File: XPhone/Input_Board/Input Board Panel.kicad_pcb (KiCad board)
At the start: 2 copper layers, 100 x 100 mm, 380 parts, among them J1 AUDIO, J10 ENV, J11 PULSE, J12 PULSE, J13 Power In, J14 Power Out, J2 AUDIO, J3 ENV, J4 ENV, J5 PULSE, J6 PULSE, J7 AUDIO, J8 AUDIO, J9 ENV, Q1 BC847CW, Q2 BC847CW, Q3 BC847CW, Q4 BC847CW, Q5 BC847CW, Q6 BC847CW, Q7 BC847CW, Q8 BC847CW, Q9 BC847CW, U1 LM833, U2 78L05, U3 TL084, U4 74HC14, U5 LM833

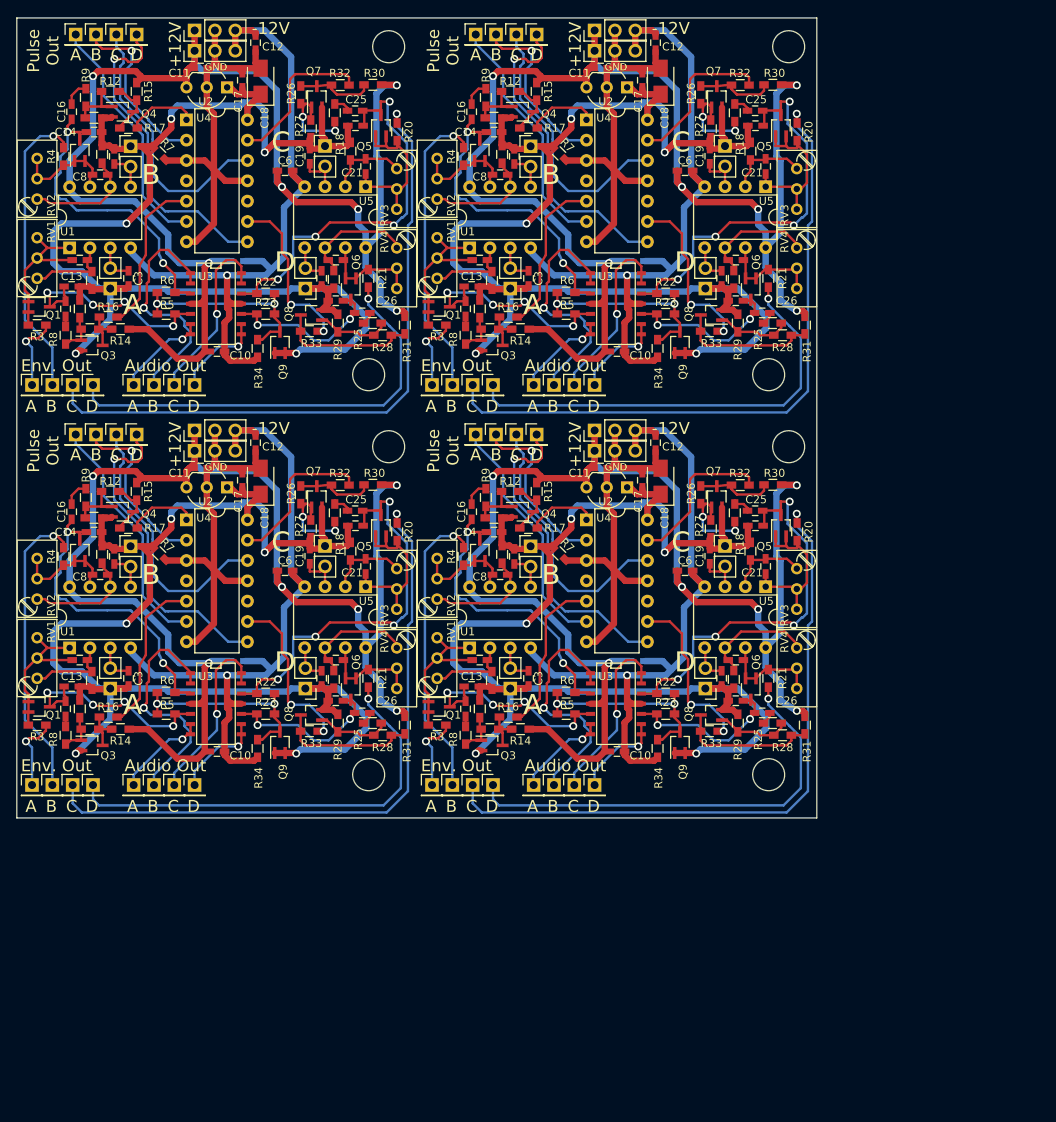
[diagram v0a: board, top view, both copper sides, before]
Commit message: fixed generation of panel
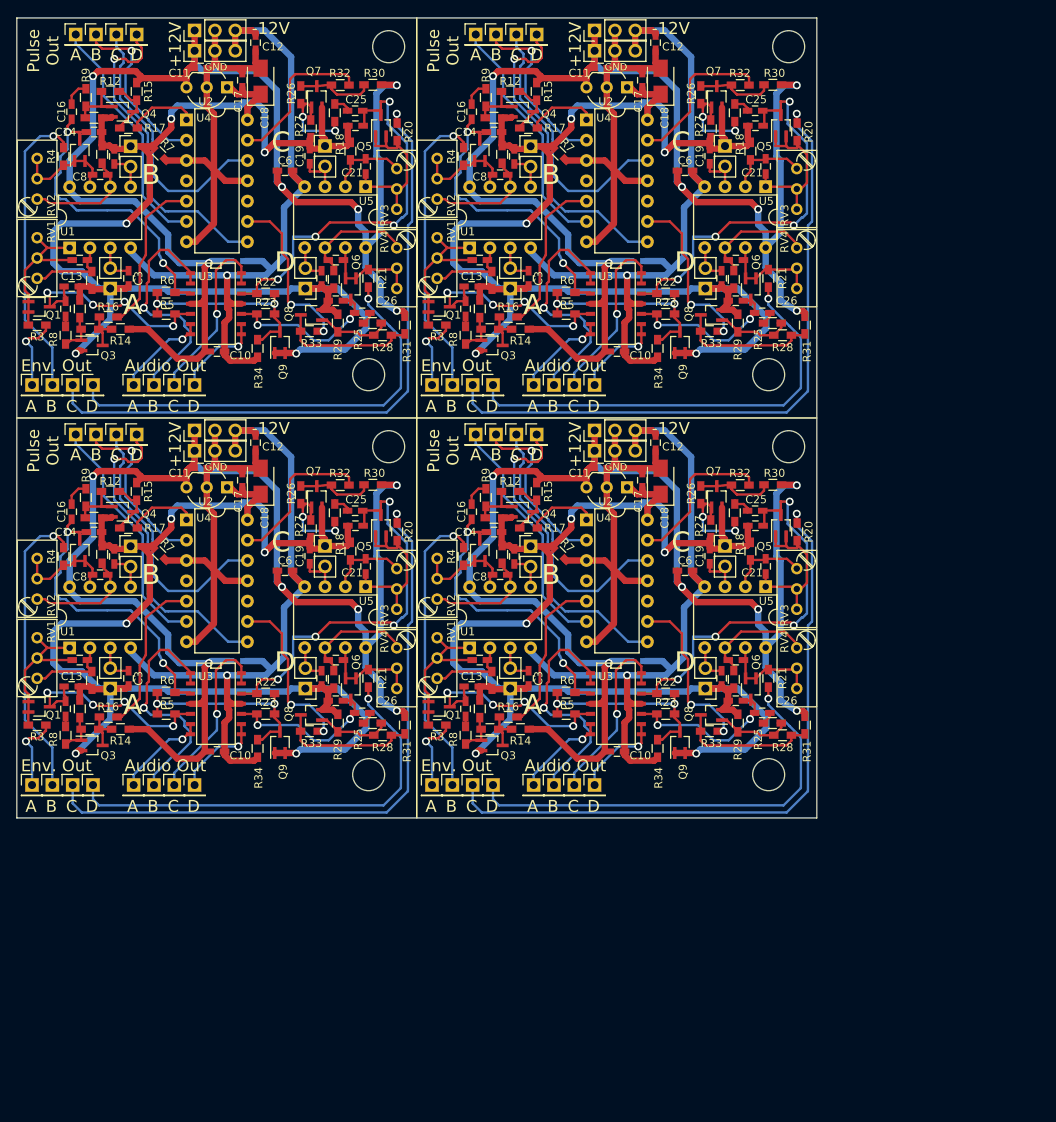
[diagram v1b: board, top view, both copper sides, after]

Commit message: optimizing XPhone/Input Board layout for cutting it into pieces; traces routed not so close to the board
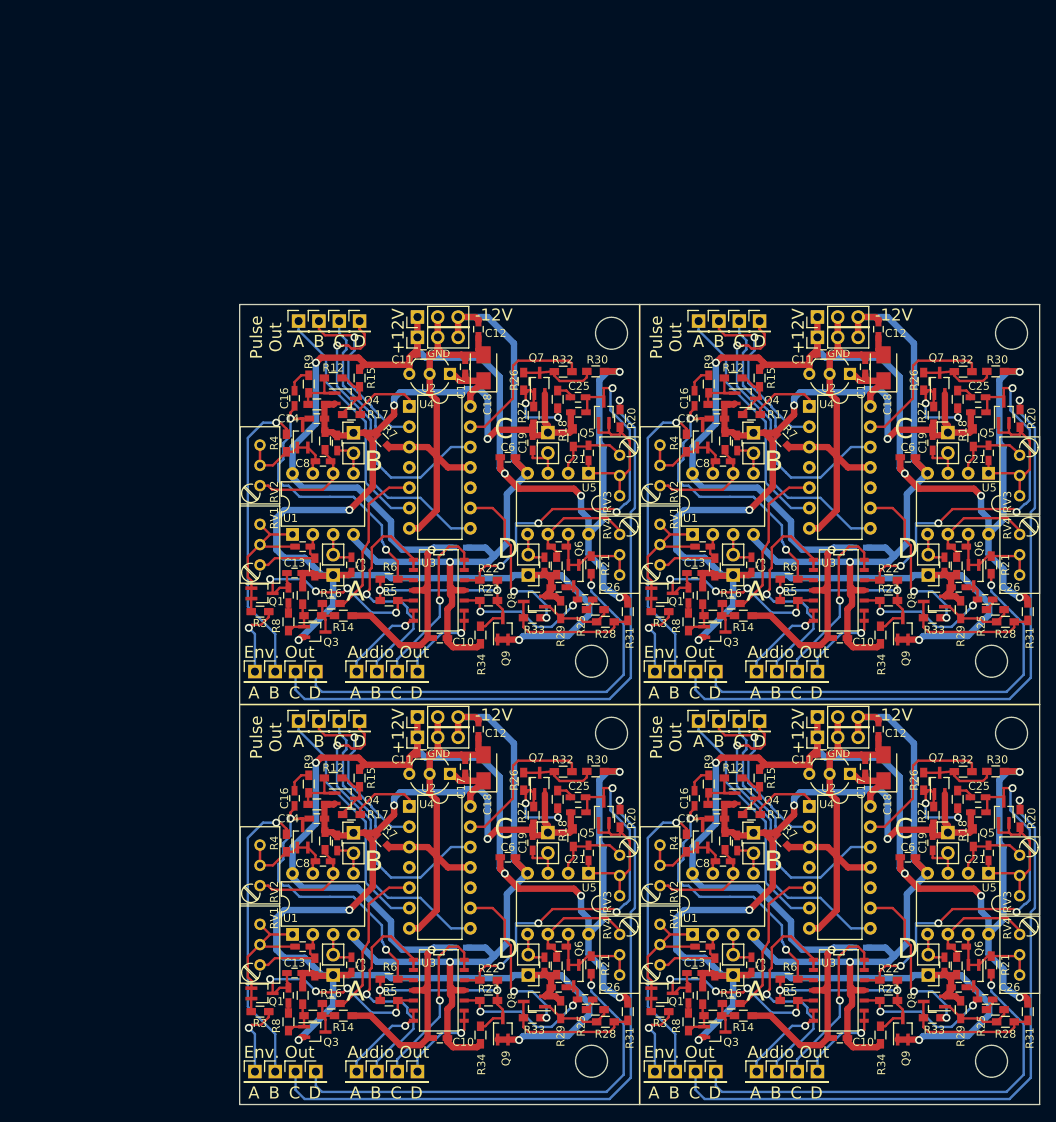
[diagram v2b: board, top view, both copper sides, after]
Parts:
- removed the C1 at (77.6, 80.4)
- removed the C1 at (27.6, 80.4)
- removed the C1 at (77.6, 30.4)
- removed the C10 at (75.0, 91.7)
- removed the C10 at (25.0, 91.7)
- removed the C10 at (75.0, 41.7)
- removed the C11 at (73.0, 56.3)
- removed the C11 at (23.0, 56.3)
- removed the C11 at (73.0, 6.26)
- removed the C12 at (79.8, 53.1)
- removed the C12 at (29.8, 53.1)
- removed the C12 at (79.8, 3.09)
- removed the C13 at (56.9, 83.6)
- removed the C13 at (6.86, 83.6)
- removed the C13 at (56.9, 33.6)
- removed the C14 at (59.7, 64.3)
- removed the C14 at (9.65, 64.3)
- removed the C14 at (59.7, 14.3)
- removed the C15 at (56.1, 86.4)
- removed the C15 at (6.10, 86.4)
- removed the C15 at (56.1, 36.4)
- removed the C16 at (56.9, 61.7)
- removed the C16 at (6.86, 61.7)
- removed the C16 at (56.9, 11.7)
- removed the C17 at (78.2, 57.8)
- removed the C17 at (28.2, 57.8)
- removed the C17 at (78.2, 7.79)
- removed the C18 at (80.5, 57.9)
- removed the C18 at (30.5, 57.9)
- removed the C18 at (80.5, 7.91)
- removed the C19 at (86.6, 67.3)
- removed the C19 at (36.6, 67.3)
- removed the C19 at (86.6, 17.3)
- removed the C20 at (88.1, 82.5)
- removed the C20 at (38.1, 82.5)
- removed the C20 at (88.1, 32.5)
- removed the C21 at (93.6, 68.6)
- removed the C21 at (43.6, 68.6)
- removed the C21 at (93.6, 18.6)
- removed the C22 at (89.9, 80.3)
- removed the C22 at (39.9, 80.3)
- removed the C22 at (89.9, 30.3)
- removed the C23 at (92.3, 63.5)
- removed the C23 at (42.3, 63.5)
- removed the C23 at (92.3, 13.5)
- removed the C24 at (89.9, 85.3)
- removed the C24 at (39.9, 85.3)
- removed the C24 at (89.9, 35.3)
- removed the C25 at (92.3, 61.6)
- removed the C25 at (42.3, 61.6)
- removed the C25 at (92.3, 11.6)
- removed the C26 at (93.2, 86.9)
- removed the C26 at (43.2, 86.9)
- removed the C26 at (93.2, 36.9)
- removed the C3 at (64.0, 82.5)
- removed the C3 at (14.0, 82.5)
- removed the C3 at (64.0, 32.5)
- removed the C4 at (62.2, 67.3)
- removed the C4 at (12.2, 67.3)
- removed the C4 at (62.2, 17.3)
- removed the C6 at (83.5, 69.1)
- removed the C6 at (33.5, 69.1)
- removed the C6 at (83.5, 19.1)
- removed the C7 at (57.9, 80.3)
- removed the C7 at (7.87, 80.3)
- removed the C7 at (57.9, 30.3)
- removed the C8 at (60.4, 69.6)
- removed the C8 at (10.4, 69.6)
- removed the C8 at (60.4, 19.6)
- removed the J1 at (51.9, 95.9)
- removed the J1 at (1.91, 95.9)
- removed the J1 at (51.9, 45.9)
- removed the J10 at (72.2, 95.9)
- removed the J10 at (22.2, 95.9)
- removed the J10 at (72.2, 45.9)
- removed the J11 at (62.4, 52.1)
- removed the J11 at (12.4, 52.1)
- removed the J11 at (62.4, 2.07)
- removed the J12 at (65.0, 52.1)
- removed the J12 at (15.0, 52.1)
- removed the J12 at (65.0, 2.07)
- removed the J13 at (72.2, 51.6)
- removed the J13 at (22.2, 51.6)
- removed the J13 at (72.2, 1.56)
- removed the J14 at (72.2, 54.1)
- removed the J14 at (22.2, 54.1)
- removed the J14 at (72.2, 4.10)
- removed the J2 at (54.4, 95.9)
- removed the J2 at (4.45, 95.9)
- removed the J2 at (54.4, 45.9)
- removed the J3 at (64.6, 95.9)
- removed the J3 at (14.6, 95.9)
- removed the J3 at (64.6, 45.9)
- removed the J4 at (67.1, 95.9)
- removed the J4 at (17.1, 95.9)
- removed the J4 at (67.1, 45.9)
- removed the J5 at (57.4, 52.1)
- removed the J5 at (7.37, 52.1)
- removed the J5 at (57.4, 2.07)
- removed the J6 at (59.9, 52.1)
- removed the J6 at (9.91, 52.1)
- removed the J6 at (59.9, 2.07)
- removed the J7 at (57.0, 95.9)
- removed the J7 at (6.99, 95.9)
- removed the J7 at (57.0, 45.9)
- removed the J8 at (59.5, 95.9)
- removed the J8 at (9.53, 95.9)
- removed the J8 at (59.5, 45.9)
- removed the J9 at (69.7, 95.9)
- removed the J9 at (19.7, 95.9)
- removed the J9 at (69.7, 45.9)
- removed the L1 at (61.7, 83.8)
- removed the L1 at (11.7, 83.8)
- removed the L1 at (61.7, 33.8)
- removed the L2 at (64.2, 66.0)
- removed the L2 at (14.2, 66.0)
- removed the L2 at (64.2, 16.0)
- removed the L3 at (88.5, 66.0)
- removed the L3 at (38.5, 66.0)
- removed the L3 at (88.5, 16.0)
- removed the L4 at (86.1, 83.8)
- removed the L4 at (36.1, 83.8)
- removed the L4 at (86.1, 33.8)
- removed the Q1 at (52.8, 86.1)
- removed the Q1 at (2.79, 86.1)
- removed the Q1 at (52.8, 36.1)
- removed the Q2 at (57.9, 66.5)
- removed the Q2 at (7.87, 66.5)
- removed the Q2 at (57.9, 16.5)
- removed the Q3 at (59.4, 90.9)
- removed the Q3 at (9.40, 90.9)
- removed the Q3 at (59.4, 40.9)
- removed the Q4 at (63.2, 61.7)
- removed the Q4 at (13.2, 61.7)
- removed the Q4 at (63.2, 11.7)
- removed the Q5 at (95.5, 63.5)
- removed the Q5 at (45.5, 63.5)
- removed the Q5 at (95.5, 13.5)
- removed the Q6 at (91.7, 83.9)
- removed the Q6 at (41.7, 83.9)
- removed the Q6 at (91.7, 33.9)
- removed the Q7 at (87.5, 59.9)
- removed the Q7 at (37.5, 59.9)
- removed the Q7 at (87.5, 9.86)
- removed the Q8 at (86.8, 87.1)
- removed the Q8 at (36.8, 87.1)
- removed the Q8 at (86.8, 37.1)
- removed the Q9 at (82.9, 90.6)
- removed the Q9 at (32.9, 90.6)
- removed the Q9 at (82.9, 40.6)
- removed the R1 at (59.4, 82.8)
- removed the R1 at (9.40, 82.8)
- removed the R1 at (59.4, 32.8)
- removed the R10 at (59.1, 88.9)
- removed the R10 at (9.14, 88.9)
- removed the R10 at (59.1, 38.9)
- removed the R11 at (57.9, 86.4)
- removed the R11 at (7.87, 86.4)
- removed the R11 at (57.9, 36.4)
- removed the R12 at (61.7, 59.2)
- removed the R12 at (11.7, 59.2)
- removed the R12 at (61.7, 9.18)
- removed the R13 at (59.7, 62.5)
- removed the R13 at (9.65, 62.5)
- removed the R13 at (59.7, 12.5)
- removed the R14 at (63.0, 88.9)
- removed the R14 at (13.0, 88.9)
- removed the R14 at (63.0, 38.9)
- removed the R15 at (65.0, 59.2)
- removed the R15 at (15.0, 59.2)
- removed the R15 at (65.0, 9.18)
- removed the R16 at (61.4, 87.4)
- removed the R16 at (11.4, 87.4)
- removed the R16 at (61.4, 37.4)
- removed the R17 at (64.0, 63.8)
- removed the R17 at (14.0, 63.8)
- removed the R17 at (64.0, 13.8)
- removed the R18 at (91.7, 66.6)
- removed the R18 at (41.7, 66.6)
- removed the R18 at (91.7, 16.6)
- removed the R19 at (89.6, 82.7)
- removed the R19 at (39.6, 82.7)
- removed the R19 at (89.6, 32.7)
- removed the R2 at (60.7, 67.1)
- removed the R2 at (10.7, 67.1)
- removed the R2 at (60.7, 17.1)
- removed the R20 at (97.5, 64.2)
- removed the R20 at (47.5, 64.2)
- removed the R20 at (97.5, 14.2)
- removed the R21 at (93.9, 82.5)
- removed the R21 at (43.9, 82.5)
- removed the R21 at (93.9, 32.5)
- removed the R22 at (81.1, 84.5)
- removed the R22 at (31.1, 84.5)
- removed the R22 at (81.1, 34.5)
- removed the R23 at (81.1, 87.0)
- removed the R23 at (31.1, 87.0)
- removed the R23 at (81.1, 37.0)
- removed the R24 at (89.8, 61.9)
- removed the R24 at (39.8, 61.9)
- removed the R24 at (89.8, 11.9)
- removed the R25 at (94.5, 88.1)
- removed the R25 at (44.5, 88.1)
- removed the R25 at (94.5, 38.1)
- removed the R26 at (85.5, 59.6)
- removed the R26 at (35.5, 59.6)
- removed the R26 at (85.5, 9.61)
- removed the R27 at (86.8, 63.9)
- removed the R27 at (36.8, 63.9)
- removed the R27 at (86.8, 13.9)
- removed the R28 at (95.7, 89.7)
- removed the R28 at (45.7, 89.7)
- removed the R28 at (95.7, 39.7)
- removed the R29 at (90.1, 88.1)
- removed the R29 at (40.1, 88.1)
- removed the R29 at (90.1, 38.1)
- removed the R3 at (52.5, 88.4)
- removed the R3 at (2.54, 88.4)
- removed the R3 at (52.5, 38.4)
- removed the R30 at (94.5, 58.4)
- removed the R30 at (44.5, 58.4)
- removed the R30 at (94.5, 8.36)
- removed the R31 at (98.5, 88.4)
- removed the R31 at (48.5, 88.4)
- removed the R31 at (98.5, 38.4)
- removed the R32 at (90.4, 58.4)
- removed the R32 at (40.4, 58.4)
- removed the R32 at (90.4, 8.39)
- removed the R33 at (86.6, 89.2)
- removed the R33 at (36.6, 89.2)
- removed the R33 at (86.6, 39.2)
- removed the R34 at (80.1, 91.3)
- removed the R34 at (30.1, 91.3)
- removed the R34 at (80.1, 41.3)
- removed the R4 at (55.8, 67.3)
- removed the R4 at (5.84, 67.3)
- removed the R4 at (55.8, 17.3)
- removed the R5 at (68.7, 87.0)
- removed the R5 at (18.7, 87.0)
- removed the R5 at (68.7, 37.0)
- removed the R6 at (68.7, 84.3)
- removed the R6 at (18.7, 84.3)
- removed the R6 at (68.7, 34.3)
- removed the R7 at (67.8, 66.9)
- removed the R7 at (17.8, 66.9)
- removed the R7 at (67.8, 16.9)
- removed the R8 at (56.1, 89.7)
- removed the R8 at (6.10, 89.7)
- removed the R8 at (56.1, 39.7)
- removed the R9 at (58.6, 59.9)
- removed the R9 at (8.64, 59.9)
- removed the R9 at (58.6, 9.94)
- removed the REF** at (94.0, 94.6)
- removed the REF** at (44.0, 94.6)
- removed the REF** at (94.0, 44.6)
- removed the REF** at (96.5, 53.6)
- removed the REF** at (46.5, 53.6)
- removed the REF** at (96.5, 3.59)
- removed the RV1 at (52.5, 82.5)
- removed the RV1 at (2.54, 82.5)
- removed the RV1 at (52.5, 32.5)
- removed the RV2 at (52.5, 72.6)
- removed the RV2 at (2.54, 72.6)
- removed the RV2 at (52.5, 22.6)
- removed the RV3 at (97.5, 68.8)
- removed the RV3 at (47.5, 68.8)
- removed the RV3 at (97.5, 18.8)
- removed the RV4 at (97.5, 78.7)
- removed the RV4 at (47.5, 78.7)
- removed the RV4 at (97.5, 28.7)
- removed the U1 at (56.6, 78.7)
- removed the U1 at (6.60, 78.7)
- removed the U1 at (56.6, 28.7)
- removed the U2 at (76.3, 58.7)
- removed the U2 at (26.3, 58.7)
- removed the U2 at (76.3, 8.67)
- removed the U3 at (75.0, 85.7)
- removed the U3 at (25.0, 85.7)
- removed the U3 at (75.0, 35.7)
- removed the U4 at (71.2, 62.7)
- removed the U4 at (21.2, 62.7)
- removed the U4 at (71.2, 12.7)
- removed the U5 at (93.6, 71.1)
- removed the U5 at (43.6, 71.1)
- removed the U5 at (93.6, 21.1)
- added C1: 10n, Capacitors_SMD:C_0603_HandSoldering, B.Cu at (105.4, 116.2)
- added C1: 10n, Capacitors_SMD:C_0603_HandSoldering, B.Cu at (55.4, 116.2)
- added C1: 10n, Capacitors_SMD:C_0603_HandSoldering, B.Cu at (105.4, 66.2)
- added C10: 10n, Capacitors_SMD:C_0603_HandSoldering, F.Cu at (102.9, 127.5)
- added C10: 10n, Capacitors_SMD:C_0603_HandSoldering, F.Cu at (52.9, 127.5)
- added C10: 10n, Capacitors_SMD:C_0603_HandSoldering, F.Cu at (102.9, 77.5)
- added C11: 10n, Capacitors_SMD:C_0603_HandSoldering, F.Cu at (100.8, 92.1)
- added C11: 10n, Capacitors_SMD:C_0603_HandSoldering, F.Cu at (50.8, 92.1)
- added C11: 10n, Capacitors_SMD:C_0603_HandSoldering, F.Cu at (100.8, 42.1)
- added C12: 10n, Capacitors_SMD:C_0603_HandSoldering, F.Cu at (107.7, 88.9)
- added C12: 10n, Capacitors_SMD:C_0603_HandSoldering, F.Cu at (57.7, 88.9)
- added C12: 10n, Capacitors_SMD:C_0603_HandSoldering, F.Cu at (107.7, 38.9)
- added C13: 10n, Capacitors_SMD:C_0603_HandSoldering, F.Cu at (84.7, 119.4)
- added C13: 10n, Capacitors_SMD:C_0603_HandSoldering, F.Cu at (34.7, 119.4)
- added C13: 10n, Capacitors_SMD:C_0603_HandSoldering, F.Cu at (84.7, 69.4)
- added C14: 10n, Capacitors_SMD:C_0603_HandSoldering, F.Cu at (87.5, 100.1)
- added C14: 10n, Capacitors_SMD:C_0603_HandSoldering, F.Cu at (37.5, 100.1)
- added C14: 10n, Capacitors_SMD:C_0603_HandSoldering, F.Cu at (87.5, 50.1)
- added C15: 10n, Capacitors_SMD:C_0603_HandSoldering, F.Cu at (84.0, 122.2)
- added C15: 10n, Capacitors_SMD:C_0603_HandSoldering, F.Cu at (34.0, 122.2)
- added C15: 10n, Capacitors_SMD:C_0603_HandSoldering, F.Cu at (84.0, 72.2)
- added C16: 10n, Capacitors_SMD:C_0603_HandSoldering, F.Cu at (84.7, 97.5)
- added C16: 10n, Capacitors_SMD:C_0603_HandSoldering, F.Cu at (34.7, 97.5)
- added C16: 10n, Capacitors_SMD:C_0603_HandSoldering, F.Cu at (84.7, 47.5)
- added C17: 10n, Capacitors_SMD:C_0603_HandSoldering, F.Cu at (106.1, 93.6)
- added C17: 10n, Capacitors_SMD:C_0603_HandSoldering, F.Cu at (56.1, 93.6)
- added C17: 10n, Capacitors_SMD:C_0603_HandSoldering, F.Cu at (106.1, 43.6)
- added C18: 10µ, Capacitors_Tantalum_SMD:CP_Tantalum_Case-B_EIA-3528-21_Wave, F.Cu at (108.3, 93.7)
- added C18: 10µ, Capacitors_Tantalum_SMD:CP_Tantalum_Case-B_EIA-3528-21_Wave, F.Cu at (58.3, 93.7)
- added C18: 10µ, Capacitors_Tantalum_SMD:CP_Tantalum_Case-B_EIA-3528-21_Wave, F.Cu at (108.3, 43.7)
- added C19: 10n, Capacitors_SMD:C_0603_HandSoldering, F.Cu at (114.5, 103.1)
- added C19: 10n, Capacitors_SMD:C_0603_HandSoldering, F.Cu at (64.5, 103.1)
- added C19: 10n, Capacitors_SMD:C_0603_HandSoldering, F.Cu at (114.5, 53.1)
- added C20: 10n, Capacitors_SMD:C_0603_HandSoldering, F.Cu at (116.0, 118.4)
- added C20: 10n, Capacitors_SMD:C_0603_HandSoldering, F.Cu at (66.0, 118.4)
- added C20: 10n, Capacitors_SMD:C_0603_HandSoldering, F.Cu at (116.0, 68.4)
- added C21: 10n, Capacitors_SMD:C_0603_HandSoldering, F.Cu at (121.5, 104.4)
- added C21: 10n, Capacitors_SMD:C_0603_HandSoldering, F.Cu at (71.5, 104.4)
- added C21: 10n, Capacitors_SMD:C_0603_HandSoldering, F.Cu at (121.5, 54.4)
- added C22: 10n, Capacitors_SMD:C_0603_HandSoldering, F.Cu at (117.7, 116.1)
- added C22: 10n, Capacitors_SMD:C_0603_HandSoldering, F.Cu at (67.7, 116.1)
- added C22: 10n, Capacitors_SMD:C_0603_HandSoldering, F.Cu at (117.7, 66.1)
- added C23: 10n, Capacitors_SMD:C_0603_HandSoldering, F.Cu at (120.2, 99.3)
- added C23: 10n, Capacitors_SMD:C_0603_HandSoldering, F.Cu at (70.2, 99.3)
- added C23: 10n, Capacitors_SMD:C_0603_HandSoldering, F.Cu at (120.2, 49.3)
- added C24: 10n, Capacitors_SMD:C_0603_HandSoldering, F.Cu at (117.7, 121.2)
- added C24: 10n, Capacitors_SMD:C_0603_HandSoldering, F.Cu at (67.7, 121.2)
- added C24: 10n, Capacitors_SMD:C_0603_HandSoldering, F.Cu at (117.7, 71.2)
- added C25: 10n, Capacitors_SMD:C_0603_HandSoldering, F.Cu at (120.2, 97.4)
- added C25: 10n, Capacitors_SMD:C_0603_HandSoldering, F.Cu at (70.2, 97.4)
- added C25: 10n, Capacitors_SMD:C_0603_HandSoldering, F.Cu at (120.2, 47.4)
- added C26: 10n, Capacitors_SMD:C_0603_HandSoldering, F.Cu at (121.0, 122.7)
- added C26: 10n, Capacitors_SMD:C_0603_HandSoldering, F.Cu at (71.0, 122.7)
- added C26: 10n, Capacitors_SMD:C_0603_HandSoldering, F.Cu at (121.0, 72.7)
- added C3: 10n, Capacitors_SMD:C_0603_HandSoldering, F.Cu at (91.8, 118.4)
- added C3: 10n, Capacitors_SMD:C_0603_HandSoldering, F.Cu at (41.8, 118.4)
- added C3: 10n, Capacitors_SMD:C_0603_HandSoldering, F.Cu at (91.8, 68.4)
- added C4: 10n, Capacitors_SMD:C_0603_HandSoldering, F.Cu at (90.1, 103.1)
- added C4: 10n, Capacitors_SMD:C_0603_HandSoldering, F.Cu at (40.1, 103.1)
- added C4: 10n, Capacitors_SMD:C_0603_HandSoldering, F.Cu at (90.1, 53.1)
- added C6: 10n, Capacitors_SMD:C_0603_HandSoldering, F.Cu at (111.4, 104.9)
- added C6: 10n, Capacitors_SMD:C_0603_HandSoldering, F.Cu at (61.4, 104.9)
- added C6: 10n, Capacitors_SMD:C_0603_HandSoldering, F.Cu at (111.4, 54.9)
- added C7: 10n, Capacitors_SMD:C_0603_HandSoldering, F.Cu at (85.7, 116.1)
- added C7: 10n, Capacitors_SMD:C_0603_HandSoldering, F.Cu at (35.7, 116.1)
- added C7: 10n, Capacitors_SMD:C_0603_HandSoldering, F.Cu at (85.7, 66.1)
- added C8: 10n, Capacitors_SMD:C_0603_HandSoldering, F.Cu at (88.3, 105.4)
- added C8: 10n, Capacitors_SMD:C_0603_HandSoldering, F.Cu at (38.3, 105.4)
- added C8: 10n, Capacitors_SMD:C_0603_HandSoldering, F.Cu at (88.3, 55.4)
- added J1: AUDIO, Pin_Headers:Pin_Header_Straight_1x01_Pitch2.54mm, F.Cu at (79.8, 131.7)
- added J1: AUDIO, Pin_Headers:Pin_Header_Straight_1x01_Pitch2.54mm, F.Cu at (29.8, 131.7)
- added J1: AUDIO, Pin_Headers:Pin_Header_Straight_1x01_Pitch2.54mm, F.Cu at (79.8, 81.7)
- added J10: ENV, Pin_Headers:Pin_Header_Straight_1x01_Pitch2.54mm, F.Cu at (100.1, 131.7)
- added J10: ENV, Pin_Headers:Pin_Header_Straight_1x01_Pitch2.54mm, F.Cu at (50.1, 131.7)
- added J10: ENV, Pin_Headers:Pin_Header_Straight_1x01_Pitch2.54mm, F.Cu at (100.1, 81.7)
- added J11: PULSE, Pin_Headers:Pin_Header_Straight_1x01_Pitch2.54mm, F.Cu at (90.3, 87.9)
- added J11: PULSE, Pin_Headers:Pin_Header_Straight_1x01_Pitch2.54mm, F.Cu at (40.3, 87.9)
- added J11: PULSE, Pin_Headers:Pin_Header_Straight_1x01_Pitch2.54mm, F.Cu at (90.3, 37.9)
- added J12: PULSE, Pin_Headers:Pin_Header_Straight_1x01_Pitch2.54mm, F.Cu at (92.8, 87.9)
- added J12: PULSE, Pin_Headers:Pin_Header_Straight_1x01_Pitch2.54mm, F.Cu at (42.8, 87.9)
- added J12: PULSE, Pin_Headers:Pin_Header_Straight_1x01_Pitch2.54mm, F.Cu at (92.8, 37.9)
- added J13: Power In, Pin_Headers:Pin_Header_Straight_1x03_Pitch2.54mm, F.Cu at (100.1, 87.4)
- added J13: Power In, Pin_Headers:Pin_Header_Straight_1x03_Pitch2.54mm, F.Cu at (50.1, 87.4)
- added J13: Power In, Pin_Headers:Pin_Header_Straight_1x03_Pitch2.54mm, F.Cu at (100.1, 37.4)
- added J14: Power Out, Pin_Headers:Pin_Header_Straight_1x03_Pitch2.54mm, F.Cu at (100.1, 89.9)
- added J14: Power Out, Pin_Headers:Pin_Header_Straight_1x03_Pitch2.54mm, F.Cu at (50.1, 89.9)
- added J14: Power Out, Pin_Headers:Pin_Header_Straight_1x03_Pitch2.54mm, F.Cu at (100.1, 39.9)
- added J2: AUDIO, Pin_Headers:Pin_Header_Straight_1x01_Pitch2.54mm, F.Cu at (82.3, 131.7)
- added J2: AUDIO, Pin_Headers:Pin_Header_Straight_1x01_Pitch2.54mm, F.Cu at (32.3, 131.7)
- added J2: AUDIO, Pin_Headers:Pin_Header_Straight_1x01_Pitch2.54mm, F.Cu at (82.3, 81.7)
- added J3: ENV, Pin_Headers:Pin_Header_Straight_1x01_Pitch2.54mm, F.Cu at (92.5, 131.7)
- added J3: ENV, Pin_Headers:Pin_Header_Straight_1x01_Pitch2.54mm, F.Cu at (42.5, 131.7)
- added J3: ENV, Pin_Headers:Pin_Header_Straight_1x01_Pitch2.54mm, F.Cu at (92.5, 81.7)
- added J4: ENV, Pin_Headers:Pin_Header_Straight_1x01_Pitch2.54mm, F.Cu at (95.0, 131.7)
- added J4: ENV, Pin_Headers:Pin_Header_Straight_1x01_Pitch2.54mm, F.Cu at (45.0, 131.7)
- added J4: ENV, Pin_Headers:Pin_Header_Straight_1x01_Pitch2.54mm, F.Cu at (95.0, 81.7)
- added J5: PULSE, Pin_Headers:Pin_Header_Straight_1x01_Pitch2.54mm, F.Cu at (85.2, 87.9)
- added J5: PULSE, Pin_Headers:Pin_Header_Straight_1x01_Pitch2.54mm, F.Cu at (35.2, 87.9)
- added J5: PULSE, Pin_Headers:Pin_Header_Straight_1x01_Pitch2.54mm, F.Cu at (85.2, 37.9)
- added J6: PULSE, Pin_Headers:Pin_Header_Straight_1x01_Pitch2.54mm, F.Cu at (87.8, 87.9)
- added J6: PULSE, Pin_Headers:Pin_Header_Straight_1x01_Pitch2.54mm, F.Cu at (37.8, 87.9)
- added J6: PULSE, Pin_Headers:Pin_Header_Straight_1x01_Pitch2.54mm, F.Cu at (87.8, 37.9)
- added J7: AUDIO, Pin_Headers:Pin_Header_Straight_1x01_Pitch2.54mm, F.Cu at (84.8, 131.7)
- added J7: AUDIO, Pin_Headers:Pin_Header_Straight_1x01_Pitch2.54mm, F.Cu at (34.8, 131.7)
- added J7: AUDIO, Pin_Headers:Pin_Header_Straight_1x01_Pitch2.54mm, F.Cu at (84.8, 81.7)
- added J8: AUDIO, Pin_Headers:Pin_Header_Straight_1x01_Pitch2.54mm, F.Cu at (87.4, 131.7)
- added J8: AUDIO, Pin_Headers:Pin_Header_Straight_1x01_Pitch2.54mm, F.Cu at (37.4, 131.7)
- added J8: AUDIO, Pin_Headers:Pin_Header_Straight_1x01_Pitch2.54mm, F.Cu at (87.4, 81.7)
- added J9: ENV, Pin_Headers:Pin_Header_Straight_1x01_Pitch2.54mm, F.Cu at (97.5, 131.7)
- added J9: ENV, Pin_Headers:Pin_Header_Straight_1x01_Pitch2.54mm, F.Cu at (47.5, 131.7)
- added J9: ENV, Pin_Headers:Pin_Header_Straight_1x01_Pitch2.54mm, F.Cu at (97.5, 81.7)
- added L1: Input Coil, Pin_Headers:Pin_Header_Straight_1x02_Pitch2.54mm, F.Cu at (89.5, 119.6)
- added L1: Input Coil, Pin_Headers:Pin_Header_Straight_1x02_Pitch2.54mm, F.Cu at (39.5, 119.6)
- added L1: Input Coil, Pin_Headers:Pin_Header_Straight_1x02_Pitch2.54mm, F.Cu at (89.5, 69.6)
- added L2: Input Coil, Pin_Headers:Pin_Header_Straight_1x02_Pitch2.54mm, F.Cu at (92.1, 101.9)
- added L2: Input Coil, Pin_Headers:Pin_Header_Straight_1x02_Pitch2.54mm, F.Cu at (42.1, 101.9)
- added L2: Input Coil, Pin_Headers:Pin_Header_Straight_1x02_Pitch2.54mm, F.Cu at (92.1, 51.9)
- added L3: Input Coil, Pin_Headers:Pin_Header_Straight_1x02_Pitch2.54mm, F.Cu at (116.4, 101.8)
- added L3: Input Coil, Pin_Headers:Pin_Header_Straight_1x02_Pitch2.54mm, F.Cu at (66.4, 101.8)
- added L3: Input Coil, Pin_Headers:Pin_Header_Straight_1x02_Pitch2.54mm, F.Cu at (116.4, 51.8)
- added L4: Input Coil, Pin_Headers:Pin_Header_Straight_1x02_Pitch2.54mm, F.Cu at (113.9, 119.6)
- added L4: Input Coil, Pin_Headers:Pin_Header_Straight_1x02_Pitch2.54mm, F.Cu at (63.9, 119.6)
- added L4: Input Coil, Pin_Headers:Pin_Header_Straight_1x02_Pitch2.54mm, F.Cu at (113.9, 69.6)
- added Q1: BC847CW, TO_SOT_Packages_SMD:SOT-323_SC-70_Handsoldering, F.Cu at (80.7, 121.9)
- added Q1: BC847CW, TO_SOT_Packages_SMD:SOT-323_SC-70_Handsoldering, F.Cu at (30.7, 121.9)
- added Q1: BC847CW, TO_SOT_Packages_SMD:SOT-323_SC-70_Handsoldering, F.Cu at (80.7, 71.9)
- added Q2: BC847CW, TO_SOT_Packages_SMD:SOT-323_SC-70_Handsoldering, F.Cu at (85.7, 102.4)
- added Q2: BC847CW, TO_SOT_Packages_SMD:SOT-323_SC-70_Handsoldering, F.Cu at (35.7, 102.4)
- added Q2: BC847CW, TO_SOT_Packages_SMD:SOT-323_SC-70_Handsoldering, F.Cu at (85.7, 52.4)
- added Q3: BC847CW, TO_SOT_Packages_SMD:SOT-323_SC-70_Handsoldering, F.Cu at (87.3, 126.8)
- added Q3: BC847CW, TO_SOT_Packages_SMD:SOT-323_SC-70_Handsoldering, F.Cu at (37.3, 126.8)
- added Q3: BC847CW, TO_SOT_Packages_SMD:SOT-323_SC-70_Handsoldering, F.Cu at (87.3, 76.8)
- added Q4: BC847CW, TO_SOT_Packages_SMD:SOT-323_SC-70_Handsoldering, F.Cu at (91.1, 97.5)
- added Q4: BC847CW, TO_SOT_Packages_SMD:SOT-323_SC-70_Handsoldering, F.Cu at (41.1, 97.5)
- added Q4: BC847CW, TO_SOT_Packages_SMD:SOT-323_SC-70_Handsoldering, F.Cu at (91.1, 47.5)
- added Q5: BC847CW, TO_SOT_Packages_SMD:SOT-323_SC-70_Handsoldering, F.Cu at (123.4, 99.3)
- added Q5: BC847CW, TO_SOT_Packages_SMD:SOT-323_SC-70_Handsoldering, F.Cu at (73.4, 99.3)
- added Q5: BC847CW, TO_SOT_Packages_SMD:SOT-323_SC-70_Handsoldering, F.Cu at (123.4, 49.3)
- added Q6: BC847CW, TO_SOT_Packages_SMD:SOT-323_SC-70_Handsoldering, F.Cu at (119.6, 119.7)
- added Q6: BC847CW, TO_SOT_Packages_SMD:SOT-323_SC-70_Handsoldering, F.Cu at (69.6, 119.7)
- added Q6: BC847CW, TO_SOT_Packages_SMD:SOT-323_SC-70_Handsoldering, F.Cu at (119.6, 69.7)
- added Q7: BC847CW, TO_SOT_Packages_SMD:SOT-323_SC-70_Handsoldering, F.Cu at (115.4, 95.7)
- added Q7: BC847CW, TO_SOT_Packages_SMD:SOT-323_SC-70_Handsoldering, F.Cu at (65.4, 95.7)
- added Q7: BC847CW, TO_SOT_Packages_SMD:SOT-323_SC-70_Handsoldering, F.Cu at (115.4, 45.7)
- added Q8: BC847CW, TO_SOT_Packages_SMD:SOT-323_SC-70_Handsoldering, F.Cu at (114.7, 122.9)
- added Q8: BC847CW, TO_SOT_Packages_SMD:SOT-323_SC-70_Handsoldering, F.Cu at (64.7, 122.9)
- added Q8: BC847CW, TO_SOT_Packages_SMD:SOT-323_SC-70_Handsoldering, F.Cu at (114.7, 72.9)
- added Q9: BC847CW, TO_SOT_Packages_SMD:SOT-323_SC-70_Handsoldering, F.Cu at (110.8, 126.4)
- added Q9: BC847CW, TO_SOT_Packages_SMD:SOT-323_SC-70_Handsoldering, F.Cu at (60.8, 126.4)
- added Q9: BC847CW, TO_SOT_Packages_SMD:SOT-323_SC-70_Handsoldering, F.Cu at (110.8, 76.4)
- added R1: 4.7, Resistors_SMD:R_0603_HandSoldering, F.Cu at (87.3, 118.6)
- added R1: 4.7, Resistors_SMD:R_0603_HandSoldering, F.Cu at (37.3, 118.6)
- added R1: 4.7, Resistors_SMD:R_0603_HandSoldering, F.Cu at (87.3, 68.6)
- added R10: 10M, Resistors_SMD:R_0603_HandSoldering, F.Cu at (87.0, 124.7)
- added R10: 10M, Resistors_SMD:R_0603_HandSoldering, F.Cu at (37.0, 124.7)
- added R10: 10M, Resistors_SMD:R_0603_HandSoldering, F.Cu at (87.0, 74.7)
- added R11: 1M, Resistors_SMD:R_0603_HandSoldering, F.Cu at (85.7, 122.2)
- added R11: 1M, Resistors_SMD:R_0603_HandSoldering, F.Cu at (35.7, 122.2)
- added R11: 1M, Resistors_SMD:R_0603_HandSoldering, F.Cu at (85.7, 72.2)
- added R12: 10M, Resistors_SMD:R_0603_HandSoldering, F.Cu at (89.5, 95.0)
- added R12: 10M, Resistors_SMD:R_0603_HandSoldering, F.Cu at (39.5, 95.0)
- added R12: 10M, Resistors_SMD:R_0603_HandSoldering, F.Cu at (89.5, 45.0)
- added R13: 1M, Resistors_SMD:R_0603_HandSoldering, F.Cu at (87.5, 98.3)
- added R13: 1M, Resistors_SMD:R_0603_HandSoldering, F.Cu at (37.5, 98.3)
- added R13: 1M, Resistors_SMD:R_0603_HandSoldering, F.Cu at (87.5, 48.3)
- added R14: 100k, Resistors_SMD:R_0603_HandSoldering, F.Cu at (90.8, 124.7)
- added R14: 100k, Resistors_SMD:R_0603_HandSoldering, F.Cu at (40.8, 124.7)
- added R14: 100k, Resistors_SMD:R_0603_HandSoldering, F.Cu at (90.8, 74.7)
- added R15: 100k, Resistors_SMD:R_0603_HandSoldering, F.Cu at (92.8, 95.0)
- added R15: 100k, Resistors_SMD:R_0603_HandSoldering, F.Cu at (42.8, 95.0)
- added R15: 100k, Resistors_SMD:R_0603_HandSoldering, F.Cu at (92.8, 45.0)
- added R16: 100k, Resistors_SMD:R_0603_HandSoldering, F.Cu at (89.3, 123.2)
- added R16: 100k, Resistors_SMD:R_0603_HandSoldering, F.Cu at (39.3, 123.2)
- added R16: 100k, Resistors_SMD:R_0603_HandSoldering, F.Cu at (89.3, 73.2)
- added R17: 100k, Resistors_SMD:R_0603_HandSoldering, F.Cu at (91.8, 99.6)
- added R17: 100k, Resistors_SMD:R_0603_HandSoldering, F.Cu at (41.8, 99.6)
- added R17: 100k, Resistors_SMD:R_0603_HandSoldering, F.Cu at (91.8, 49.6)
- added R18: 4.7, Resistors_SMD:R_0603_HandSoldering, F.Cu at (119.6, 102.5)
- added R18: 4.7, Resistors_SMD:R_0603_HandSoldering, F.Cu at (69.6, 102.5)
- added R18: 4.7, Resistors_SMD:R_0603_HandSoldering, F.Cu at (119.6, 52.5)
- added R19: 4.7, Resistors_SMD:R_0603_HandSoldering, F.Cu at (117.5, 118.5)
- added R19: 4.7, Resistors_SMD:R_0603_HandSoldering, F.Cu at (67.5, 118.5)
- added R19: 4.7, Resistors_SMD:R_0603_HandSoldering, F.Cu at (117.5, 68.5)
- added R2: 4.7, Resistors_SMD:R_0603_HandSoldering, F.Cu at (88.5, 102.9)
- added R2: 4.7, Resistors_SMD:R_0603_HandSoldering, F.Cu at (38.5, 102.9)
- added R2: 4.7, Resistors_SMD:R_0603_HandSoldering, F.Cu at (88.5, 52.9)
- added R20: 10k, Resistors_SMD:R_0603_HandSoldering, F.Cu at (125.4, 100.1)
- added R20: 10k, Resistors_SMD:R_0603_HandSoldering, F.Cu at (75.4, 100.1)
- added R20: 10k, Resistors_SMD:R_0603_HandSoldering, F.Cu at (125.4, 50.1)
- added R21: 10k, Resistors_SMD:R_0603_HandSoldering, F.Cu at (121.8, 118.4)
- added R21: 10k, Resistors_SMD:R_0603_HandSoldering, F.Cu at (71.8, 118.4)
- added R21: 10k, Resistors_SMD:R_0603_HandSoldering, F.Cu at (121.8, 68.4)
- added R22: 10M, Resistors_SMD:R_0603_HandSoldering, F.Cu at (109.0, 120.3)
- added R22: 10M, Resistors_SMD:R_0603_HandSoldering, F.Cu at (59.0, 120.3)
- added R22: 10M, Resistors_SMD:R_0603_HandSoldering, F.Cu at (109.0, 70.3)
- added R23: 10M, Resistors_SMD:R_0603_HandSoldering, F.Cu at (109.0, 122.8)
- added R23: 10M, Resistors_SMD:R_0603_HandSoldering, F.Cu at (59.0, 122.8)
- added R23: 10M, Resistors_SMD:R_0603_HandSoldering, F.Cu at (109.0, 72.8)
- added R24: 1M, Resistors_SMD:R_0603_HandSoldering, F.Cu at (117.6, 97.7)
- added R24: 1M, Resistors_SMD:R_0603_HandSoldering, F.Cu at (67.6, 97.7)
- added R24: 1M, Resistors_SMD:R_0603_HandSoldering, F.Cu at (117.6, 47.7)
- added R25: 1M, Resistors_SMD:R_0603_HandSoldering, F.Cu at (122.3, 124.0)
- added R25: 1M, Resistors_SMD:R_0603_HandSoldering, F.Cu at (72.3, 124.0)
- added R25: 1M, Resistors_SMD:R_0603_HandSoldering, F.Cu at (122.3, 74.0)
- added R26: 10M, Resistors_SMD:R_0603_HandSoldering, F.Cu at (113.4, 95.4)
- added R26: 10M, Resistors_SMD:R_0603_HandSoldering, F.Cu at (63.4, 95.4)
- added R26: 10M, Resistors_SMD:R_0603_HandSoldering, F.Cu at (113.4, 45.4)
- added R27: 1M, Resistors_SMD:R_0603_HandSoldering, F.Cu at (114.6, 99.7)
- added R27: 1M, Resistors_SMD:R_0603_HandSoldering, F.Cu at (64.6, 99.7)
- added R27: 1M, Resistors_SMD:R_0603_HandSoldering, F.Cu at (114.6, 49.7)
- added R28: 10M, Resistors_SMD:R_0603_HandSoldering, F.Cu at (123.6, 125.5)
- added R28: 10M, Resistors_SMD:R_0603_HandSoldering, F.Cu at (73.6, 125.5)
- added R28: 10M, Resistors_SMD:R_0603_HandSoldering, F.Cu at (123.6, 75.5)
- added R29: 1M, Resistors_SMD:R_0603_HandSoldering, F.Cu at (118.0, 124.0)
- added R29: 1M, Resistors_SMD:R_0603_HandSoldering, F.Cu at (68.0, 124.0)
- added R29: 1M, Resistors_SMD:R_0603_HandSoldering, F.Cu at (118.0, 74.0)
- added R3: 10k, Resistors_SMD:R_0603_HandSoldering, F.Cu at (80.4, 124.2)
- added R3: 10k, Resistors_SMD:R_0603_HandSoldering, F.Cu at (30.4, 124.2)
- added R3: 10k, Resistors_SMD:R_0603_HandSoldering, F.Cu at (80.4, 74.2)
- added R30: 100k, Resistors_SMD:R_0603_HandSoldering, F.Cu at (122.4, 94.2)
- added R30: 100k, Resistors_SMD:R_0603_HandSoldering, F.Cu at (72.4, 94.2)
- added R30: 100k, Resistors_SMD:R_0603_HandSoldering, F.Cu at (122.4, 44.2)
- added R31: 100k, Resistors_SMD:R_0603_HandSoldering, F.Cu at (126.4, 124.2)
- added R31: 100k, Resistors_SMD:R_0603_HandSoldering, F.Cu at (76.4, 124.2)
- added R31: 100k, Resistors_SMD:R_0603_HandSoldering, F.Cu at (126.4, 74.2)
- added R32: 100k, Resistors_SMD:R_0603_HandSoldering, F.Cu at (118.3, 94.2)
- added R32: 100k, Resistors_SMD:R_0603_HandSoldering, F.Cu at (68.3, 94.2)
- added R32: 100k, Resistors_SMD:R_0603_HandSoldering, F.Cu at (118.3, 44.2)
- added R33: 100k, Resistors_SMD:R_0603_HandSoldering, F.Cu at (114.4, 125.0)
- added R33: 100k, Resistors_SMD:R_0603_HandSoldering, F.Cu at (64.4, 125.0)
- added R33: 100k, Resistors_SMD:R_0603_HandSoldering, F.Cu at (114.4, 75.0)
- added R34: 10k, Resistors_SMD:R_0603_HandSoldering, F.Cu at (108.0, 127.1)
- added R34: 10k, Resistors_SMD:R_0603_HandSoldering, F.Cu at (58.0, 127.1)
- added R34: 10k, Resistors_SMD:R_0603_HandSoldering, F.Cu at (108.0, 77.1)
- added R4: 10k, Resistors_SMD:R_0603_HandSoldering, F.Cu at (83.7, 103.1)
- added R4: 10k, Resistors_SMD:R_0603_HandSoldering, F.Cu at (33.7, 103.1)
- added R4: 10k, Resistors_SMD:R_0603_HandSoldering, F.Cu at (83.7, 53.1)
- added R5: 10M, Resistors_SMD:R_0603_HandSoldering, F.Cu at (96.5, 122.8)
- added R5: 10M, Resistors_SMD:R_0603_HandSoldering, F.Cu at (46.5, 122.8)
- added R5: 10M, Resistors_SMD:R_0603_HandSoldering, F.Cu at (96.5, 72.8)
- added R6: 10M, Resistors_SMD:R_0603_HandSoldering, F.Cu at (96.5, 120.1)
- added R6: 10M, Resistors_SMD:R_0603_HandSoldering, F.Cu at (46.5, 120.1)
- added R6: 10M, Resistors_SMD:R_0603_HandSoldering, F.Cu at (96.5, 70.1)
- added R7: 0, Resistors_SMD:R_0603_HandSoldering, F.Cu at (95.6, 102.7)
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
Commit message: creating panel and gerbers
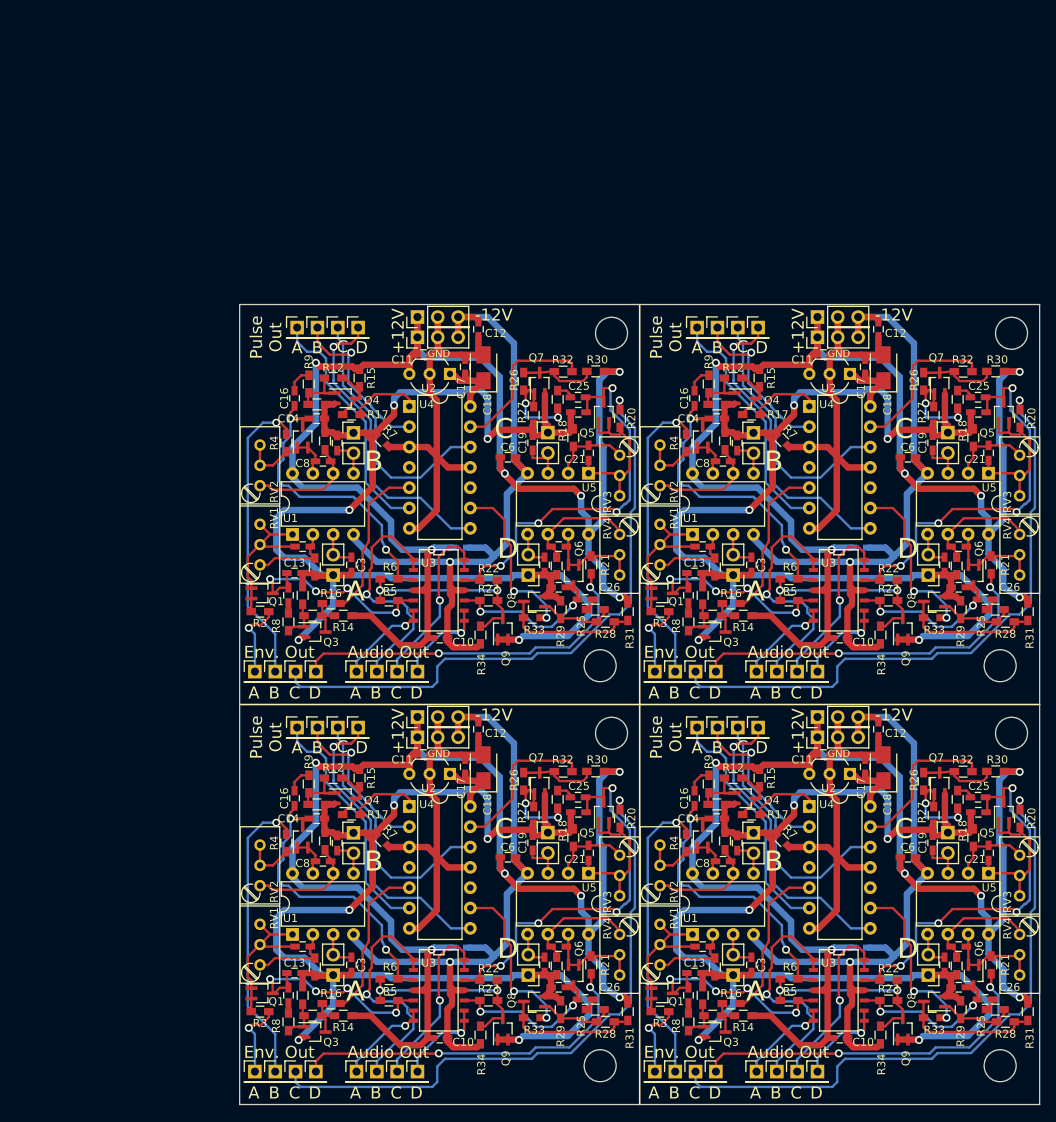
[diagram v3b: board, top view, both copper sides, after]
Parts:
- removed the J11 at (90.3, 87.9)
- removed the J11 at (40.3, 87.9)
- removed the J11 at (90.3, 37.9)
- removed the J12 at (92.8, 87.9)
- removed the J12 at (42.8, 87.9)
- removed the J12 at (92.8, 37.9)
- removed the J5 at (85.2, 87.9)
- removed the J5 at (35.2, 87.9)
- removed the J5 at (85.2, 37.9)
- removed the J6 at (87.8, 87.9)
- removed the J6 at (37.8, 87.9)
- removed the J6 at (87.8, 37.9)
- removed the REF** at (121.8, 130.4)
- removed the REF** at (71.8, 130.4)
- removed the REF** at (121.8, 80.4)
- added J11: PULSE, Pin_Headers:Pin_Header_Straight_1x01_Pitch2.54mm, F.Cu at (90.1, 88.7)
- added J11: PULSE, Pin_Headers:Pin_Header_Straight_1x01_Pitch2.54mm, F.Cu at (40.1, 88.7)
- added J11: PULSE, Pin_Headers:Pin_Header_Straight_1x01_Pitch2.54mm, F.Cu at (90.1, 38.7)
- added J12: PULSE, Pin_Headers:Pin_Header_Straight_1x01_Pitch2.54mm, F.Cu at (92.7, 88.7)
- added J12: PULSE, Pin_Headers:Pin_Header_Straight_1x01_Pitch2.54mm, F.Cu at (42.7, 88.7)
- added J12: PULSE, Pin_Headers:Pin_Header_Straight_1x01_Pitch2.54mm, F.Cu at (92.7, 38.7)
- added J5: PULSE, Pin_Headers:Pin_Header_Straight_1x01_Pitch2.54mm, F.Cu at (85.0, 88.7)
- added J5: PULSE, Pin_Headers:Pin_Header_Straight_1x01_Pitch2.54mm, F.Cu at (35.0, 88.7)
- added J5: PULSE, Pin_Headers:Pin_Header_Straight_1x01_Pitch2.54mm, F.Cu at (85.0, 38.7)
- added J6: PULSE, Pin_Headers:Pin_Header_Straight_1x01_Pitch2.54mm, F.Cu at (87.6, 88.7)
- added J6: PULSE, Pin_Headers:Pin_Header_Straight_1x01_Pitch2.54mm, F.Cu at (37.6, 88.7)
- added J6: PULSE, Pin_Headers:Pin_Header_Straight_1x01_Pitch2.54mm, F.Cu at (87.6, 38.7)
- added REF**: MountingHole_4mm, Screw_Holes:#6, F.Cu at (122.9, 131.0)
- added REF**: MountingHole_4mm, Screw_Holes:#6, F.Cu at (72.9, 131.0)
- added REF**: MountingHole_4mm, Screw_Holes:#6, F.Cu at (122.9, 81.0)
- moved REF** 1.21 mm to (72.9, 81.0)
- moved J11 0.83 mm to (40.1, 38.7)
- moved J12 0.83 mm to (42.7, 38.7)
- moved J5 0.83 mm to (35.0, 38.7)
- moved J6 0.83 mm to (37.6, 38.7)
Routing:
- net Net-(J8-Pad1): track 223.1 -> 179.6 mm, vias 4 -> 8
- net Net-(J7-Pad1): track 330.5 -> 305.8 mm
- net Net-(J12-Pad1): track 162.2 -> 153.2 mm
- net Net-(J6-Pad1): track 87.5 -> 83.0 mm
- net Net-(J11-Pad1): track 136.3 -> 132.0 mm
- net +12V: track 669.0 -> 665.2 mm
- net Net-(J5-Pad1): track 121.8 -> 122.4 mm
